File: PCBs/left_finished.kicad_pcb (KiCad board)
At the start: 2 copper layers, 147.2 x 118.7 mm, 68 parts

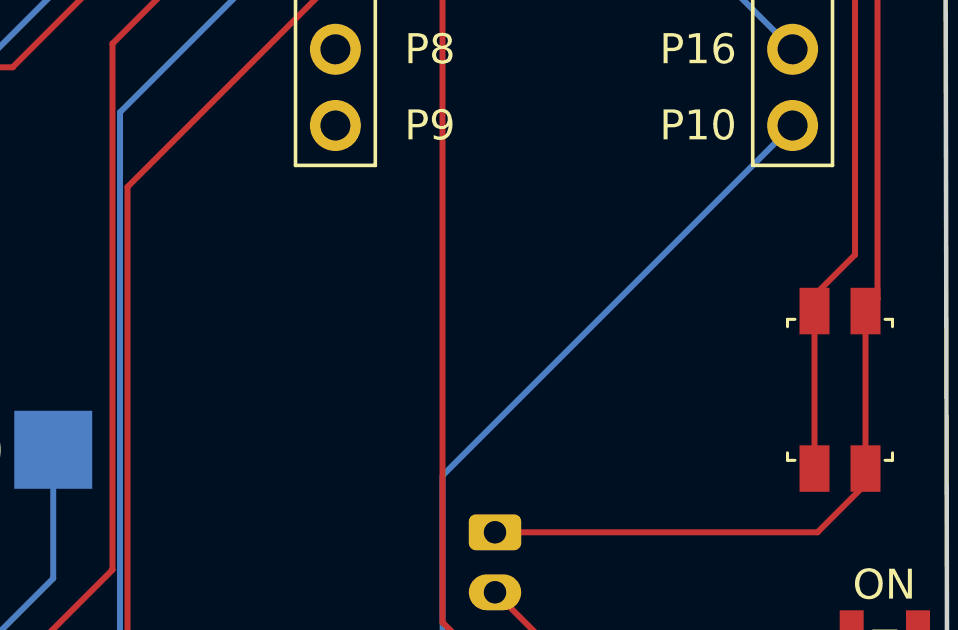
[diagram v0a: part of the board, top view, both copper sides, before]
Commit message: file(3D): move to the root folder / feat(add): Add image to the PCBs
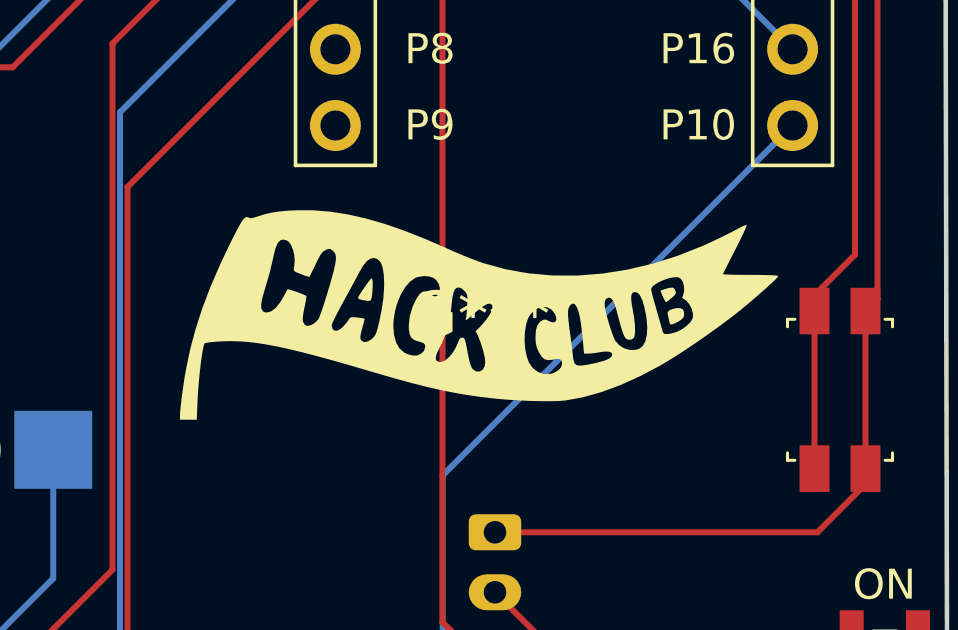
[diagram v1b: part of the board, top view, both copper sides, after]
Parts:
- added G***: LOGO, PCBs:flag, F.Cu at (170.0, 141.8)
